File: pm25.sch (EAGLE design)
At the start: 33 parts, among them J1 CON-0024, Q1 TRANSISTOR-NPN-40V-0.2A-SOT23, Q2 TR-0001, U1 IC-0010, U2 CCS811B-JOPD500, U3 POWER-SWITCH-SIP32509DT', U4 SI7021-A20-GM1R

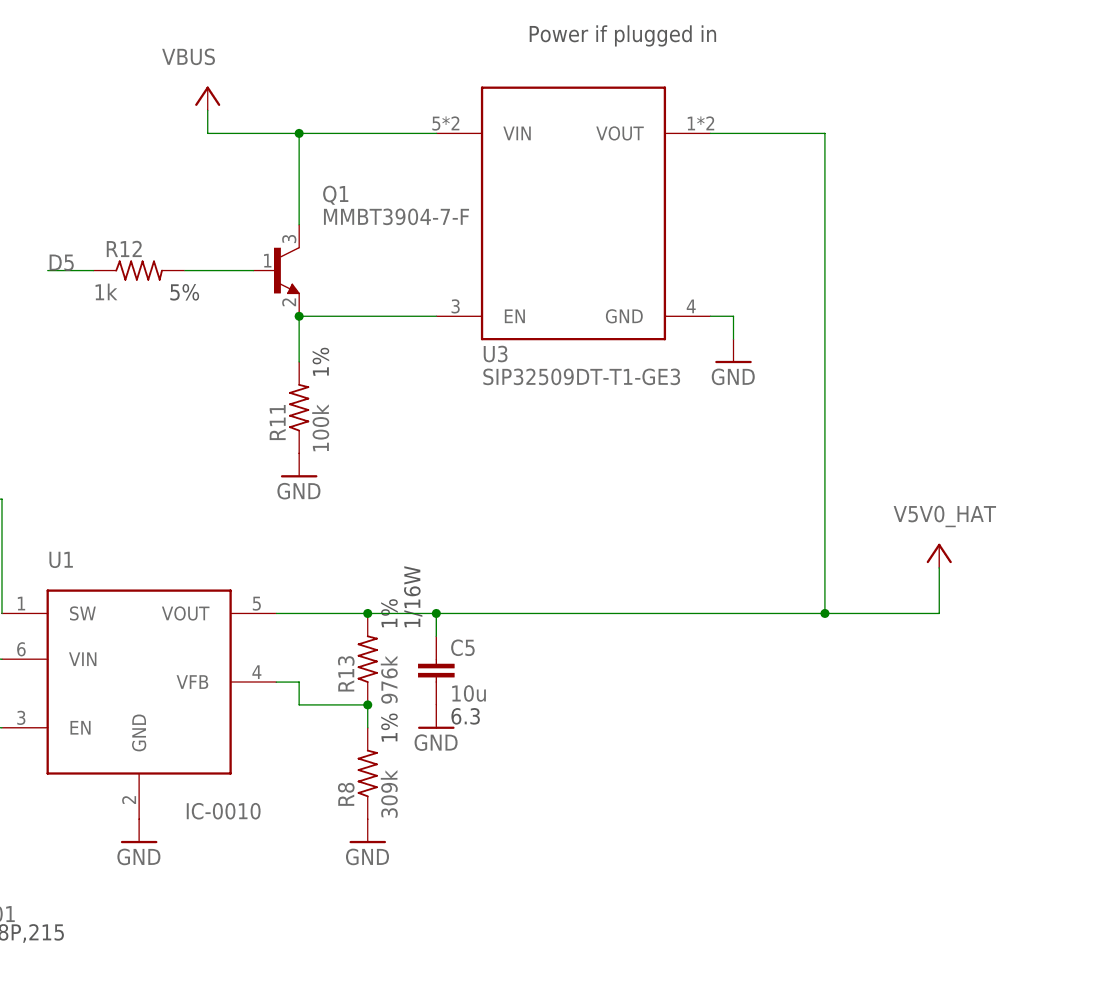
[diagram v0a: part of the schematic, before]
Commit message: Slight hardware update. Substitute MCP1640 on U1 Add L2 Add TP1
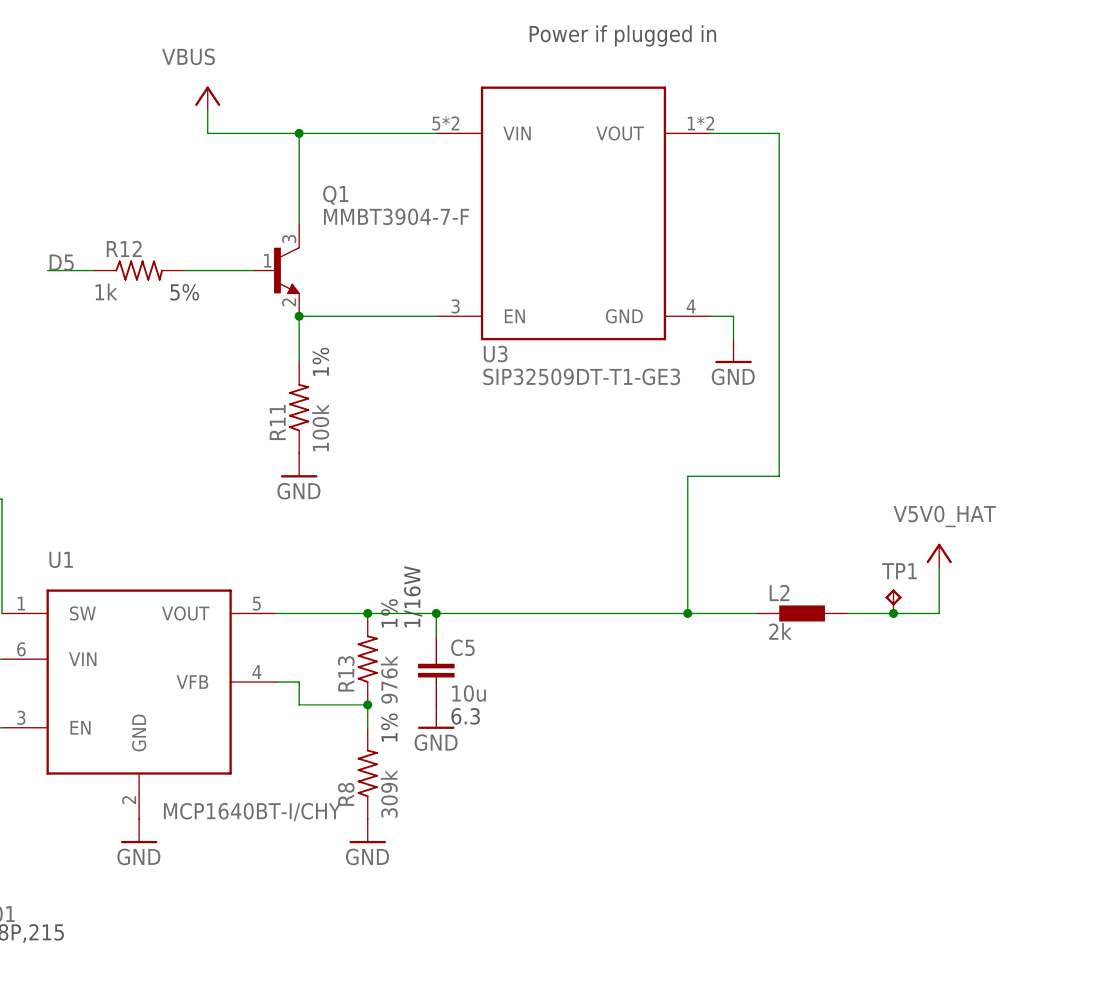
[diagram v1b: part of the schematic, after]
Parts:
- added L2: 2k, wolff-den:FERRITE-0805
- added TP1: TP, wolff-den:TP
- U1: value IC-0010 -> POWER-VREG-FB-EN-SW-350MA; device wolff-den:IC-0010 -> wolff-den:POWER-VREG-FB-EN-SW-350MA
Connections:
- new net V5V0_BEAD: C5.1, L2.1, R13.2, U1.VOUT, U3.VOUT
- net V5V0_HAT: now also L2.2, TP1.TP; no longer C5.1, R13.2, U1.VOUT, U3.VOUT
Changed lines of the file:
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@@
 <layer number="112" name="tSilk" color="7" fill="1" visible="yes" active="yes"/>
 <layer number="113" name="ReferenceLS" color="7" fill="1" visible="no" active="no"/>
+<layer number="114" name="Badge_Outline" color="7" fill="1" visible="yes" active="yes"/>
+<layer number="115" name="ReferenceISLANDS" color="7" fill="1" visible="yes" active="yes"/>
 <layer number="116" name="Patch_BOT" color="9" fill="4" visible="yes" active="yes"/>
 <layer number="118" name="Rect_Pads" color="7" fill="1" visible="no" active="no"/>
@@
 </attributes>
 <variantdefs>
-<variantdef name="Production" current="yes"/>
+<variantdef name="Production"/>
 </variantdefs>
 <classes>
@@
 <part name="+3V2" library="supply1" library_urn="urn:adsk.eagle:library:371" deviceset="+3V3" device=""/>
 <part name="GND1" library="supply1" library_urn="urn:adsk.eagle:library:371" deviceset="GND" device=""/>
-<part name="U1" library="wolff-den" library_urn="urn:adsk.eagle:library:6370453" deviceset="IC-0010" device="" package3d_urn="urn:adsk.eagle:package:5807329/2"/>
+<part name="U1" library="wolff-den" library_urn="urn:adsk.eagle:library:6370453" deviceset="POWER-VREG-FB-EN-SW" device="" package3d_urn="urn:adsk.eagle:package:5807329/2" technology="-350MA" value="POWER-VREG-FB-EN-SW-350MA"/>
 <part name="GND2" library="supply1" library_urn="urn:adsk.eagle:library:371" deviceset="GND" device=""/>
 <part name="P+3" library="wolff-den" library_urn="urn:adsk.eagle:library:6370453" deviceset="VBUS" device=""/>
@@
 <part name="R12" library="wolff-den" library_urn="urn:adsk.eagle:library:6370453" deviceset="RES-0039" device="" package3d_urn="urn:adsk.eagle:package:5807335/2" value="1k"/>
 <part name="R13" library="wolff-den" library_urn="urn:adsk.eagle:library:6370453" deviceset="RES" device="-0402" package3d_urn="urn:adsk.eagle:package:5807335/2" technology="-976K-1%" value="976k"/>
+<part name="L2" library="wolff-den" library_urn="urn:adsk.eagle:library:6370453" deviceset="FERRITE" device="-0805" package3d_urn="urn:adsk.eagle:package:5807318/2" value="2k"/>
+<part name="TP1" library="wolff-den" library_urn="urn:adsk.eagle:library:6370453" deviceset="TP" device="" package3d_urn="urn:adsk.eagle:package:5807313/4"/>
 </parts>
 <sheets>
@@
 <instance part="U1" gate="G$1" x="121.92" y="193.04" smashed="yes">
 <attribute name="NAME" x="111.76" y="205.74" size="1.778" layer="95"/>
-<attribute name="VALUE" x="127" y="177.8" size="1.778" layer="96"/>
+<attribute name="MPN" x="124.46" y="177.8" size="1.778" layer="96"/>
 </instance>
 <instance part="GND2" gate="1" x="121.92" y="175.26" smashed="yes">
@@
 <attribute name="POWER" x="153.162" y="198.882" size="1.778" layer="97" rot="R90"/>
 </instance>
+<instance part="L2" gate="G$1" x="195.58" y="200.66" smashed="yes">
+<attribute name="NAME" x="191.77" y="202.0316" size="1.778" layer="95"/>
+<attribute name="VALUE" x="191.77" y="197.739" size="1.778" layer="96"/>
+</instance>
+<instance part="TP1" gate="G$1" x="205.74" y="203.2" smashed="yes">
+<attribute name="NAME" x="204.47" y="204.47" size="1.778" layer="95"/>
+</instance>
 </instances>
 <busses>
@@
 <net name="V5V0_HAT" class="0">
 <segment>
-<wire x1="198.12" y1="254" x2="198.12" y2="200.66" width="0.1524" layer="91"/>
 <pinref part="P+8" gate="G$1" pin="V5V0_HAT"/>
-<wire x1="198.12" y1="200.66" x2="210.82" y2="200.66" width="0.1524" layer="91"/>
+<wire x1="205.74" y1="200.66" x2="210.82" y2="200.66" width="0.1524" layer="91"/>
 <wire x1="210.82" y1="200.66" x2="210.82" y2="205.74" width="0.1524" layer="91"/>
-<pinref part="U1" gate="G$1" pin="VOUT"/>
-<wire x1="154.94" y1="200.66" x2="147.32" y2="200.66" width="0.1524" layer="91"/>
-<wire x1="147.32" y1="200.66" x2="137.16" y2="200.66" width="0.1524" layer="91"/>
-<wire x1="154.94" y1="198.12" x2="154.94" y2="200.66" width="0.1524" layer="91"/>
-<pinref part="C5" gate="A" pin="1"/>
-<wire x1="154.94" y1="200.66" x2="198.12" y2="200.66" width="0.1524" layer="91"/>
-<junction x="154.94" y="200.66"/>
-<junction x="198.12" y="200.66"/>
-<wire x1="185.42" y1="254" x2="198.12" y2="254" width="0.1524" layer="91"/>
-<pinref part="U3" gate="G$1" pin="VOUT"/>
-<pinref part="R13" gate="G$1" pin="2"/>
-<junction x="147.32" y="200.66"/>
+<pinref part="L2" gate="G$1" pin="2"/>
+<wire x1="200.66" y1="200.66" x2="205.74" y2="200.66" width="0.1524" layer="91"/>
+<pinref part="TP1" gate="G$1" pin="TP"/>
+<junction x="205.74" y="200.66"/>
 </segment>
 <segment>
@@
 </segment>
 </net>
+<net name="V5V0_BEAD" class="0">
+<segment>
+<pinref part="U1" gate="G$1" pin="VOUT"/>
+<pinref part="C5" gate="A" pin="1"/>
+<wire x1="154.94" y1="198.12" x2="154.94" y2="200.66" width="0.1524" layer="91"/>
+<wire x1="154.94" y1="200.66" x2="147.32" y2="200.66" width="0.1524" layer="91"/>
+<pinref part="R13" gate="G$1" pin="2"/>
+<junction x="147.32" y="200.66"/>
+<wire x1="147.32" y1="200.66" x2="137.16" y2="200.66" width="0.1524" layer="91"/>
+<pinref part="L2" gate="G$1" pin="1"/>
+<wire x1="190.5" y1="200.66" x2="182.88" y2="200.66" width="0.1524" layer="91"/>
+<junction x="154.94" y="200.66"/>
+<wire x1="182.88" y1="200.66" x2="154.94" y2="200.66" width="0.1524" layer="91"/>
+<wire x1="185.42" y1="254" x2="193.04" y2="254" width="0.1524" layer="91"/>
+<pinref part="U3" gate="G$1" pin="VOUT"/>
+<wire x1="193.04" y1="254" x2="193.04" y2="215.9" width="0.1524" layer="91"/>
+<wire x1="193.04" y1="215.9" x2="182.88" y2="215.9" width="0.1524" layer="91"/>
+<wire x1="182.88" y1="215.9" x2="182.88" y2="200.66" width="0.1524" layer="91"/>
+<junction x="182.88" y="200.66"/>
+</segment>
+</net>

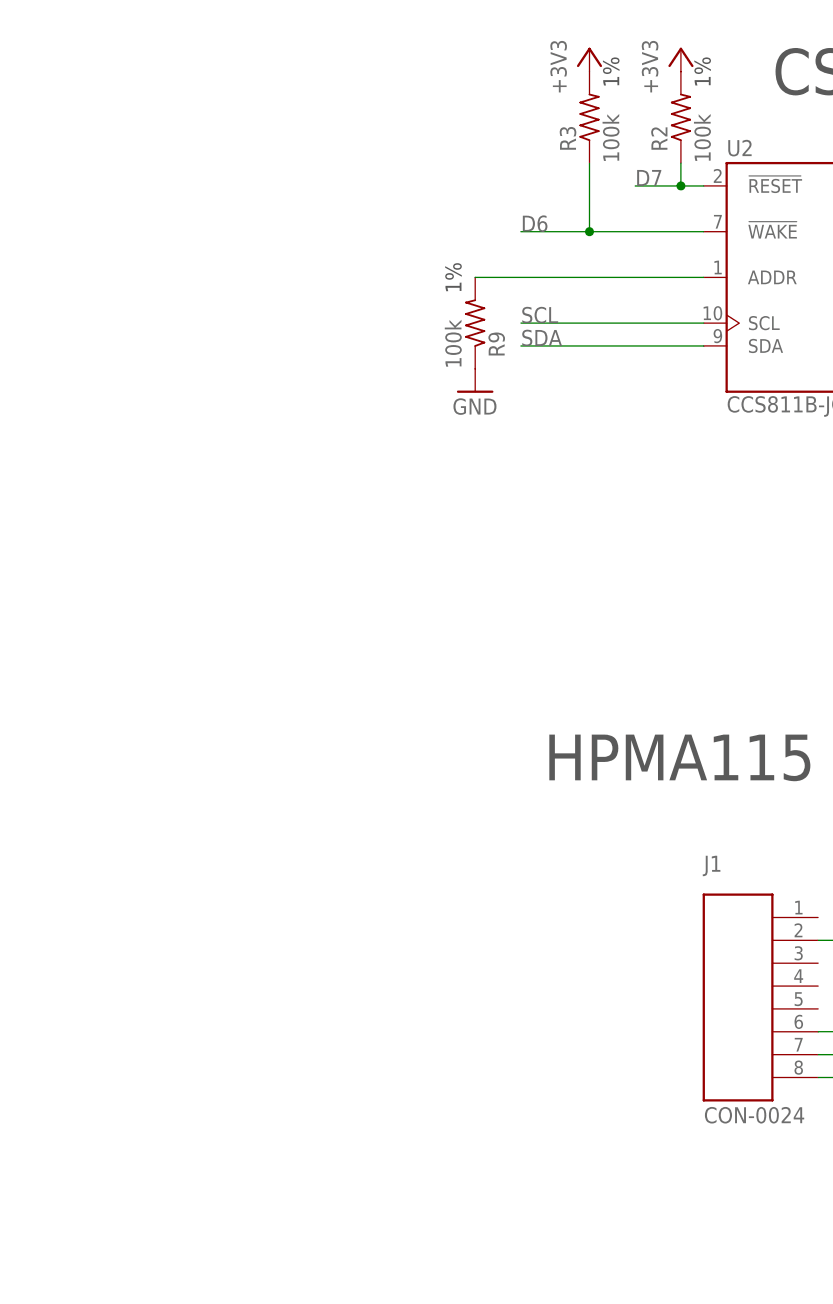
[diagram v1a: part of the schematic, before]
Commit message: Replacing connection from D7 with D5 (so the LED isn't always on)
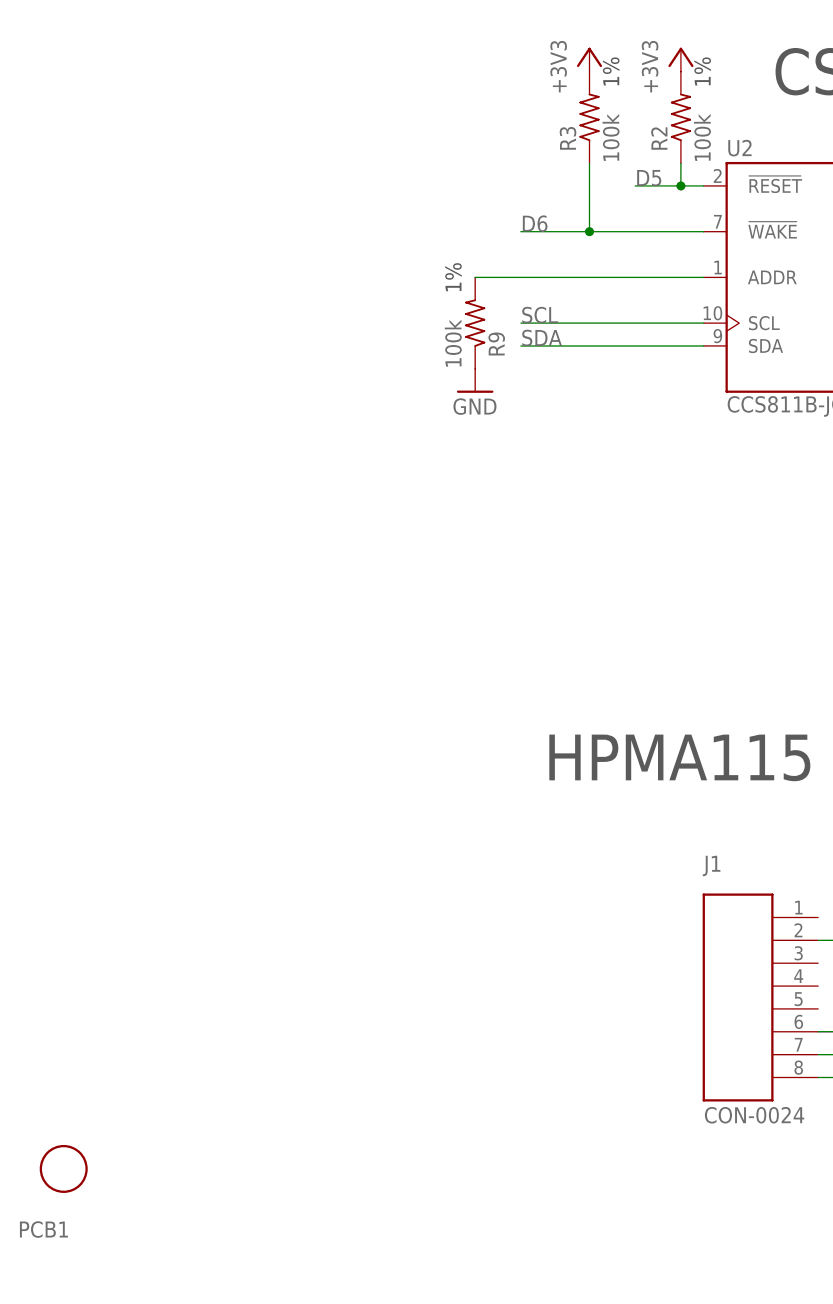
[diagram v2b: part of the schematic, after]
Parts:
- added PCB1: PCB-PS-CCS811-SI7021, wolff-den:PCB-PS-CCS811-SI7021
- U3: value POWER-SWITCH-SIP32509DT' -> POWER-SWITCH-SIP32509DT; device wolff-den:POWER-SWITCH-SIP32509DT' -> wolff-den:POWER-SWITCH-SIP32509DT
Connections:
- net D5: now also R2.1, U2.!RESET
- net D7: no longer R2.1, U2.!RESET
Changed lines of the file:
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@@
 </attributes>
 <variantdefs>
-<variantdef name="Production"/>
+<variantdef name="Production" current="yes"/>
 </variantdefs>
 <classes>
@@
 <part name="P+1" library="wolff-den" library_urn="urn:adsk.eagle:library:6370453" deviceset="VBUS" device=""/>
 <part name="GND13" library="supply1" library_urn="urn:adsk.eagle:library:371" deviceset="GND" device=""/>
-<part name="U3" library="wolff-den" library_urn="urn:adsk.eagle:library:6370453" deviceset="POWER-SWITCH" device="-SIP32509DT'" package3d_urn="urn:adsk.eagle:package:5807329/2"/>
+<part name="U3" library="wolff-den" library_urn="urn:adsk.eagle:library:6370453" deviceset="POWER-SWITCH" device="-SIP32509DT" package3d_urn="urn:adsk.eagle:package:5807329/2"/>
 <part name="Q1" library="wolff-den" library_urn="urn:adsk.eagle:library:6370453" deviceset="TRANSISTOR" device="-SOT23" package3d_urn="urn:adsk.eagle:package:5807332/3" technology="-NPN-40V-0.2A"/>
 <part name="R11" library="wolff-den" library_urn="urn:adsk.eagle:library:6370453" deviceset="RES-0041" device="" package3d_urn="urn:adsk.eagle:package:5807335/2" value="100k"/>
@@
 <part name="L2" library="wolff-den" library_urn="urn:adsk.eagle:library:6370453" deviceset="FERRITE" device="-0805" package3d_urn="urn:adsk.eagle:package:5807318/2" value="2k"/>
 <part name="TP1" library="wolff-den" library_urn="urn:adsk.eagle:library:6370453" deviceset="TP" device="" package3d_urn="urn:adsk.eagle:package:5807313/4"/>
+<part name="PCB1" library="wolff-den" library_urn="urn:adsk.eagle:library:6370453" deviceset="PCB" device="" technology="-PS-CCS811-SI7021"/>
 </parts>
 <sheets>
@@
 <attribute name="NAME" x="204.47" y="204.47" size="1.778" layer="95"/>
 </instance>
+<instance part="PCB1" gate="G$1" x="15.24" y="12.7" smashed="yes">
+<attribute name="NAME" x="10.16" y="5.08" size="1.778" layer="95"/>
+</instance>
 </instances>
 <busses>
@@
 <label x="309.88" y="137.16" size="1.778" layer="95"/>
 <pinref part="JP2" gate="G$1" pin="5"/>
-</segment>
-<segment>
-<wire x1="86.36" y1="121.92" x2="83.82" y2="121.92" width="0.1524" layer="91"/>
-<label x="78.74" y="121.92" size="1.778" layer="95"/>
-<pinref part="U2" gate="G$1" pin="!RESET"/>
-<pinref part="R2" gate="A" pin="1"/>
-<wire x1="83.82" y1="121.92" x2="78.74" y2="121.92" width="0.1524" layer="91"/>
-<wire x1="83.82" y1="124.46" x2="83.82" y2="121.92" width="0.1524" layer="91"/>
-<junction x="83.82" y="121.92"/>
 </segment>
 </net>
@@
 <pinref part="R12" gate="A" pin="1"/>
 </segment>
-</net>
+<segment>
+<wire x1="86.36" y1="121.92" x2="83.82" y2="121.92" width="0.1524" layer="91"/>
+<label x="78.74" y="121.92" size="1.778" layer="95"/>
+<pinref part="U2" gate="G$1" pin="!RESET"/>
+<pinref part="R2" gate="A" pin="1"/>
+<wire x1="83.82" y1="121.92" x2="78.74" y2="121.92" width="0.1524" layer="91"/>
+<wire x1="83.82" y1="124.46" x2="83.82" y2="121.92" width="0.1524" layer="91"/>
+<junction x="83.82" y="121.92"/>
+</segment>
+</net>
